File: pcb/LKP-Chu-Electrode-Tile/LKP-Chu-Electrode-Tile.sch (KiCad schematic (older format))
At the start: 19 parts, among them J1 Intercon, J10 Electrode 0, J11 Electrode 2, J12 Electrode 4, J13 Electrode 6, J14 Electrode 8, J15 Electrode 10, J16 Electrode 12, J17 Electrode 14, J2 Electrode 1, J3 Electrode 3, J4 Electrode 5, J5 Electrode 7, J6 Electrode 9, J7 Electrode 11, J8 Electrode 13, J9 Electrode 15

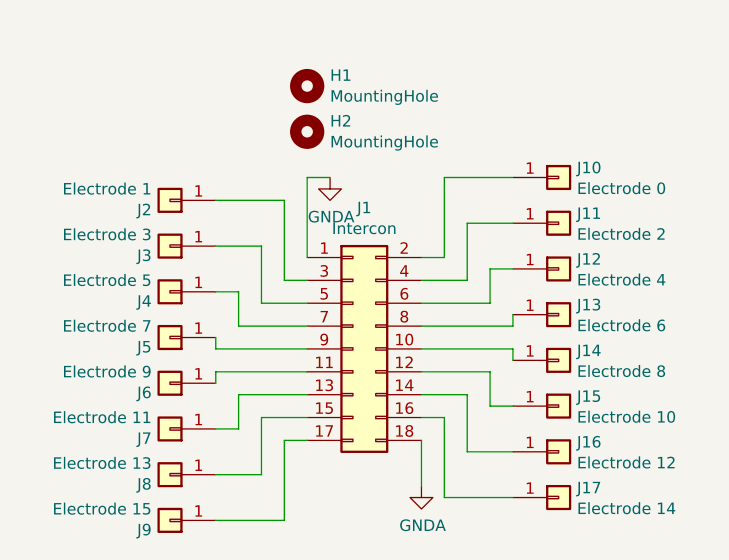
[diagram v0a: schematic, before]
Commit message: Place screw holes.
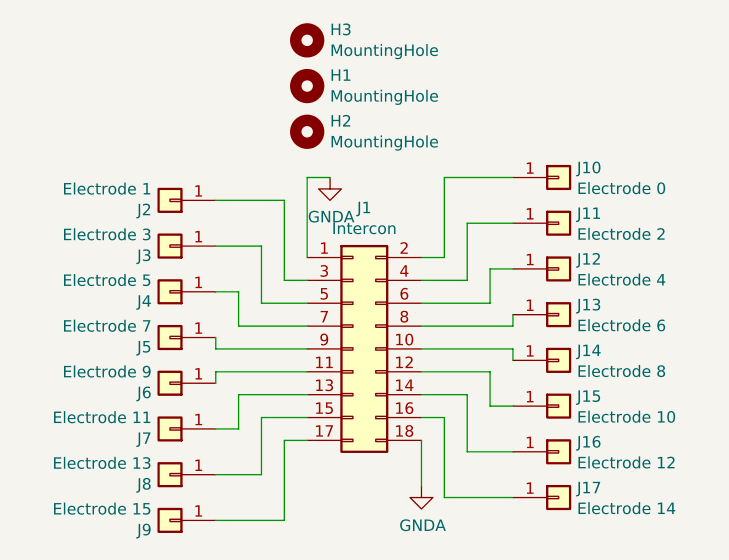
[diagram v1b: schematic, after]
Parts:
- added H3: MountingHole, MountingHole:MountingHole_3.2mm_M3_ISO7380, symbol Mechanical:MountingHole
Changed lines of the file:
@@
 Wire Wire Line
 	6300 4850 6300 5050
+$Comp
+L Mechanical:MountingHole H3
+U 1 1 5E349CFA
+P 5800 3100
+F 0 "H3" H 5900 3146 50  0000 L CNN
+F 1 "MountingHole" H 5900 3055 50  0000 L CNN
+F 2 "MountingHole:MountingHole_3.2mm_M3_ISO7380" H 5800 3100 50  0001 C CNN
+F 3 "~" H 5800 3100 50  0001 C CNN
+	1    5800 3100
+	1    0    0    -1
+$EndComp
 $EndSCHEMATC
